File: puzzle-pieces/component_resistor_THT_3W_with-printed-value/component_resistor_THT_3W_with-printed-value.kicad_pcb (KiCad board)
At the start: 2 copper layers, 40 x 40 mm, 7 parts, among them J1 Conn_01x02_Pin, J5 Conn_01x02_Pin

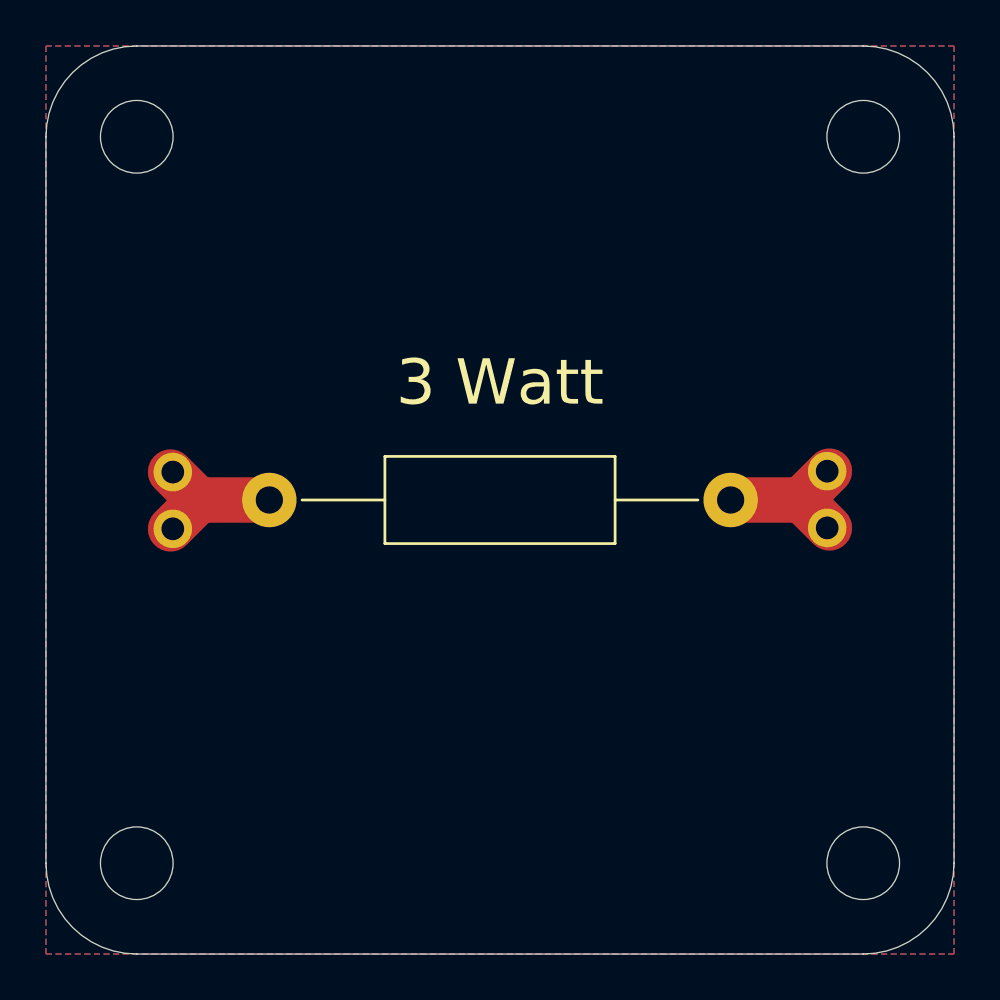
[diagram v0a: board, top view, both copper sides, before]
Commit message: Update resistor footprints and add THT 3W production files
Replaced mounting hole footprints with SMD resistor footprints in the SMT E-6 series panel and updated net assignments. Added new KiCad PCB, project, and production ZIP files for the THT 3W E-6 series resistors. Updated connector reference and position in the SMT panel.
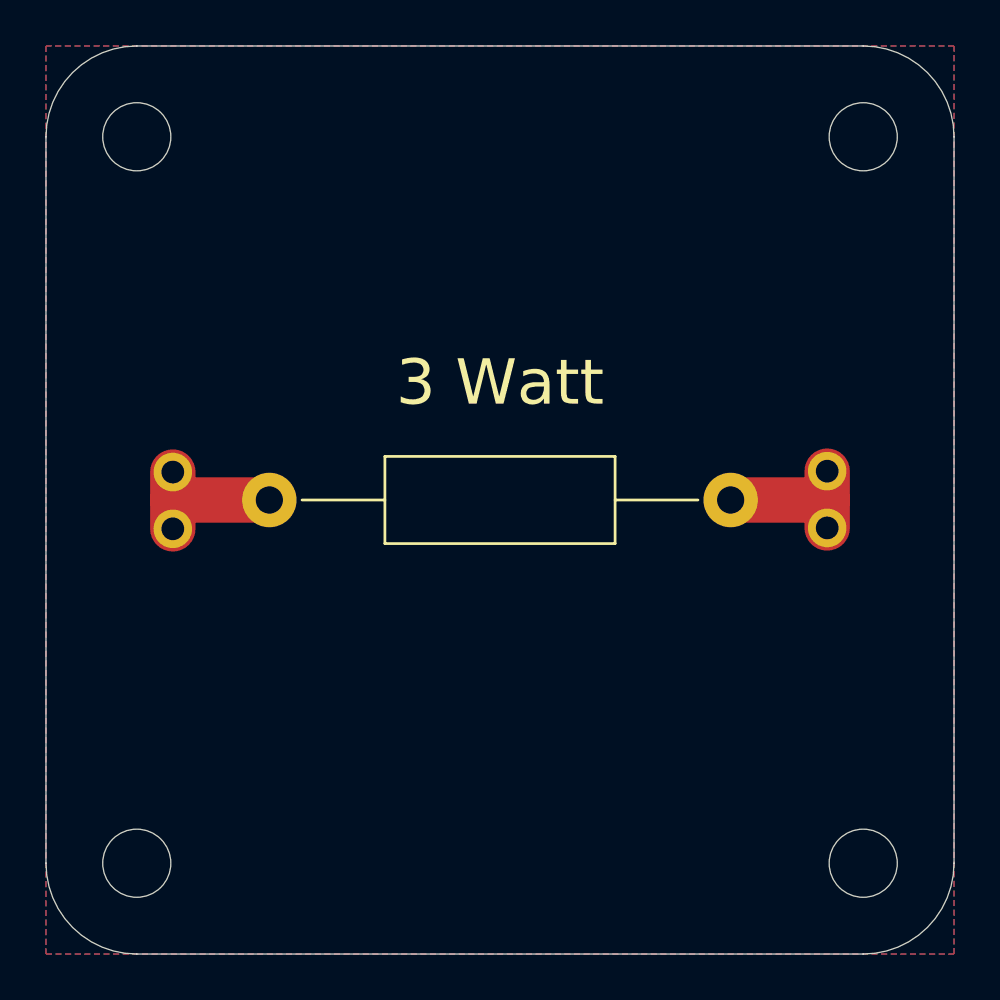
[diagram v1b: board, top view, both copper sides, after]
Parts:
- H1, H2, H3, H4: footprint MountingHole:MountingHole_3.2mm_M3 -> EASYEDA2KICAD:MountingHole_3.0mm_M3_tight
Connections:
- net NordSued renamed Net-(J5-Pin_1)
